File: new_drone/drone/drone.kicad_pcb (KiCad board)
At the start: 2 copper layers, 28 parts, among them J1 Conn_01x06, SW1 SW_Push_Open, SW2 SW_Push_Open, U1 MPU-6050, U2 ESP32-WROOM-32, U3 TPS63001, U4 BMP280, U5 MCP8063, U6 MCP8063, U7 MCP8063, U8 MCP8063

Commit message: add pcb cut
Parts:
- moved J1 15.4 mm to (161.3, 85.2), turned to 180 degrees
- moved U2 15.2 mm to (149.2, 79.4)
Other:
- board outline added: 100 x 100 mm
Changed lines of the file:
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@@
   )
   (footprint "RF_Module:ESP32-WROOM-32" (layer "F.Cu")
-    (at 134.431 75.699)
+    (at 149.155 79.385)
     (descr "Single 2.4 GHz Wi-Fi and Bluetooth combo chip https://www.espressif.com/sites/default/files/documentation/esp32-wroom-32_datasheet_en.pdf")
     (tags "Single 2.4 GHz Wi-Fi and Bluetooth combo  chip")
@@
       (polygon
         (pts
-          (xy 110.431 65.899)
-          (xy 158.431 65.899)
-          (xy 158.431 44.959)
-          (xy 110.431 44.959)
+          (xy 125.155 69.585)
+          (xy 173.155 69.585)
+          (xy 173.155 48.645)
+          (xy 125.155 48.645)
         )
       )
@@
   )
   (footprint "Connector_PinHeader_2.54mm:PinHeader_1x06_P2.54mm_Vertical" (layer "F.Cu")
-    (at 161.281 69.759)
+    (at 161.281 85.16 180)
     (descr "Through hole straight pin header, 1x06, 2.54mm pitch, single row")
     (tags "Through hole pin header THT 1x06 2.54mm single row")
@@
     (fp_line (start 1.27 13.97) (end -1.27 13.97)
       (stroke (width 0.1) (type solid)) (layer "F.Fab"))
-    (pad "1" thru_hole rect (at 0 0) (size 1.7 1.7) (drill 1) (layers "*.Cu" "*.Mask")
+    (pad "1" thru_hole rect (at 0 0 180) (size 1.7 1.7) (drill 1) (layers "*.Cu" "*.Mask")
       (net 1 "GND") (pinfunction "Pin_1") (pintype "passive"))
-    (pad "2" thru_hole oval (at 0 2.54) (size 1.7 1.7) (drill 1) (layers "*.Cu" "*.Mask")
+    (pad "2" thru_hole oval (at 0 2.54 180) (size 1.7 1.7) (drill 1) (layers "*.Cu" "*.Mask")
       (net 8 "unconnected-(J1-Pin_2-Pad2)") (pinfunction "Pin_2") (pintype "passive"))
-    (pad "3" thru_hole oval (at 0 5.08) (size 1.7 1.7) (drill 1) (layers "*.Cu" "*.Mask")
+    (pad "3" thru_hole oval (at 0 5.08 180) (size 1.7 1.7) (drill 1) (layers "*.Cu" "*.Mask")
       (net 2 "VCC") (pinfunction "Pin_3") (pintype "passive"))
-    (pad "4" thru_hole oval (at 0 7.62) (size 1.7 1.7) (drill 1) (layers "*.Cu" "*.Mask")
+    (pad "4" thru_hole oval (at 0 7.62 180) (size 1.7 1.7) (drill 1) (layers "*.Cu" "*.Mask")
       (net 9 "ESP_RX") (pinfunction "Pin_4") (pintype "passive"))
-    (pad "5" thru_hole oval (at 0 10.16) (size 1.7 1.7) (drill 1) (layers "*.Cu" "*.Mask")
+    (pad "5" thru_hole oval (at 0 10.16 180) (size 1.7 1.7) (drill 1) (layers "*.Cu" "*.Mask")
       (net 10 "ESP_TX") (pinfunction "Pin_5") (pintype "passive"))
-    (pad "6" thru_hole oval (at 0 12.7) (size 1.7 1.7) (drill 1) (layers "*.Cu" "*.Mask")
+    (pad "6" thru_hole oval (at 0 12.7 180) (size 1.7 1.7) (drill 1) (layers "*.Cu" "*.Mask")
       (net 11 "unconnected-(J1-Pin_6-Pad6)") (pinfunction "Pin_6") (pintype "passive"))
     (model "${KICAD6_3DMODEL_DIR}/Connector_PinHeader_2.54mm.3dshapes/PinHeader_1x06_P2.54mm_Vertical.wrl"
@@
     )
   )
+  (gr_line (start 100 145) (end 100 135)
+    (stroke (width 0.1) (type default)) (layer "Edge.Cuts"))
+  (gr_line (start 100 135) (end 120 115)
+    (stroke (width 0.1) (type default)) (layer "Edge.Cuts"))
+  (gr_line (start 200 65) (end 200 55)
+    (stroke (width 0.1) (type default)) (layer "Edge.Cuts"))
+  (gr_line (start 185 50) (end 165 70)
+    (stroke (width 0.1) (type default)) (layer "Edge.Cuts"))
+  (gr_line (start 200 55) (end 195 50)
+    (stroke (width 0.1) (type default)) (layer "Edge.Cuts"))
+  (gr_line (start 100 65) (end 100 55)
+    (stroke (width 0.1) (type default)) (layer "Edge.Cuts"))
+  (gr_line (start 200 145) (end 195 150)
+    (stroke (width 0.1) (type default)) (layer "Edge.Cuts"))
+  (gr_line (start 120 115) (end 120 85)
+    (stroke (width 0.1) (type default)) (layer "Edge.Cuts"))
+  (gr_line (start 135 70) (end 165 70)
+    (stroke (width 0.1) (type default)) (layer "Edge.Cuts"))
+  (gr_line (start 200 135) (end 200 145)
+    (stroke (width 0.1) (type default)) (layer "Edge.Cuts"))
+  (gr_line (start 180 85) (end 200 65)
+    (stroke (width 0.1) (type default)) (layer "Edge.Cuts"))
+  (gr_line (start 120 85) (end 100 65)
+    (stroke (width 0.1) (type default)) (layer "Edge.Cuts"))
+  (gr_line (start 105 50) (end 115 50)
+    (stroke (width 0.1) (type default)) (layer "Edge.Cuts"))
+  (gr_line (start 115 150) (end 105 150)
+    (stroke (width 0.1) (type default)) (layer "Edge.Cuts"))
+  (gr_line (start 105 150) (end 100 145)
+    (stroke (width 0.1) (type default)) (layer "Edge.Cuts"))
+  (gr_line (start 135 130) (end 115 150)
+    (stroke (width 0.1) (type default)) (layer "Edge.Cuts"))
+  (gr_line (start 180 115) (end 200 135)
+    (stroke (width 0.1) (type default)) (layer "Edge.Cuts"))
+  (gr_line (start 195 150) (end 185 150)
+    (stroke (width 0.1) (type default)) (layer "Edge.Cuts"))
+  (gr_line (start 100 55) (end 105 50)
+    (stroke (width 0.1) (type default)) (layer "Edge.Cuts"))
+  (gr_line (start 165 130) (end 135 130)
+    (stroke (width 0.1) (type default)) (layer "Edge.Cuts"))
+  (gr_line (start 195 50) (end 185 50)
+    (stroke (width 0.1) (type default)) (layer "Edge.Cuts"))
+  (gr_line (start 115 50) (end 135 70)
+    (stroke (width 0.1) (type default)) (layer "Edge.Cuts"))
+  (gr_line (start 185 150) (end 165 130)
+    (stroke (width 0.1) (type default)) (layer "Edge.Cuts"))
+  (gr_line (start 180 85) (end 180 115)
+    (stroke (width 0.1) (type default)) (layer "Edge.Cuts"))
   (gr_line (start 150 75) (end 175 50)
     (stroke (width 0.15) (type default)) (layer "User.1"))

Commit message: first wiring
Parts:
- removed R5: 100, Resistor_SMD:R_0603_1608Metric
- removed U3: TPS63001, Package_SON:Texas_DRC0010J_ThermalVias
- removed U6, U7, U8: MCP8063, Package_DFN_QFN:DFN-8-1EP_4x4mm_P0.8mm_EP2.5x3.6mm
- added TP1: TestPoint, TestPoint:TestPoint_Pad_3.0x3.0mm, F.Cu at (176.8, 73.3)
- added TP2: TestPoint, TestPoint:TestPoint_Pad_3.0x3.0mm, F.Cu at (180.3, 76.8)
- added TP3: TestPoint, TestPoint:TestPoint_Pad_3.0x3.0mm, F.Cu at (173.2, 69.7)
- C4, C5, C6: value 0.1uF -> C
- D1: moved to B.Cu
- moved C1 45.7 mm to (155.5, 101.8), turned to 180 degrees
- moved C2 44.6 mm to (155.5, 100.0)
- moved C3 43.9 mm to (155.5, 98.2)
- moved R7 35.0 mm to (154.8, 94.1), turned to -90 degrees
- moved R6 33.6 mm to (153.0, 94.1), turned to -90 degrees
- moved U5 32.4 mm to (171.3, 78.4), turned to -135 degrees
- moved C5 31.6 mm to (136.8, 117.5)
- moved C4 31.6 mm to (136.8, 115.0)
- moved C6 31.6 mm to (136.8, 120.0)
- moved R1 31.6 mm to (140.8, 110.0)
- moved R4 31.6 mm to (140.8, 117.5)
- moved C7 31.6 mm to (140.8, 107.5)
- moved R2 31.6 mm to (140.8, 112.5)
- moved R3 31.6 mm to (140.8, 115.0)
- moved D1 21.5 mm to (150.0, 72.9), turned to 180 degrees
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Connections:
- C4 pad 1: Net-(U3-EN) -> +BATT
- C5 pad 1: VCC -> +BATT
- C6 pad 1: VCC -> Net-(U5-Vbias)
- U5 pad 2: unconnected-(U5-Vbias-Pad2) -> Net-(U5-Vbias)
- U5 pad 3: unconnected-(U5-OUT1-Pad3) -> Net-(U5-OUT1)
- U5 pad 4: unconnected-(U5-OUT2-Pad4) -> Net-(U5-OUT2)
- U5 pad 5: unconnected-(U5-GND-Pad5) -> GND
- U5 pad 6: unconnected-(U5-OUT3-Pad6) -> Net-(U5-OUT3)
- U5 pad 7: unconnected-(U5-VDD-Pad7) -> +BATT
- U5 pad 8: unconnected-(U5-PWM-Pad8) -> MOTOR_1
- U5 pad 9: unconnected-(U5-GND-Pad9) -> GND
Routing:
- net VCC: track 0.00 -> 14.2 mm, vias 0 -> 2
- net Net-(U5-OUT3): track 0.00 -> 14.0 mm, vias 0 -> 2
- net Net-(U5-OUT1): track 0.00 -> 9.38 mm
- net Net-(U1-REGOUT): track 0.00 -> 9.14 mm
- net Net-(U5-OUT2): track 0.00 -> 6.93 mm
- net Net-(U4-SDO): track 0.00 -> 6.66 mm
- net SDA: track 0.00 -> 5.54 mm
- net Net-(U1-CPOUT): track 0.00 -> 4.77 mm
- net ESP_RX: track 0.00 -> 3.68 mm
- net ESP_TX: track 0.00 -> 3.41 mm
- net SCL: track 0.00 -> 3.35 mm
- net Net-(U4-CSB): track 0.00 -> 3.10 mm
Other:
- outline, holes or cut-outs redrawn

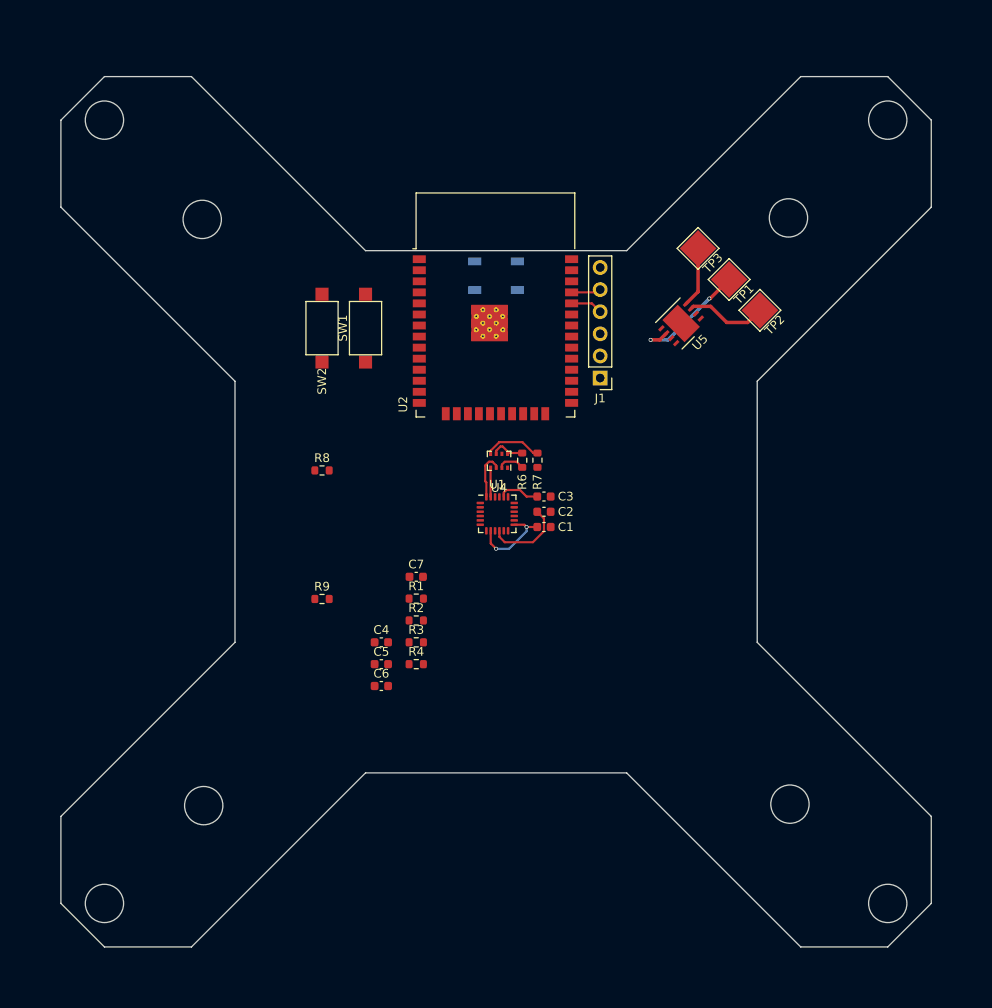
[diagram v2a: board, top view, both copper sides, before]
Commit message: add regulator
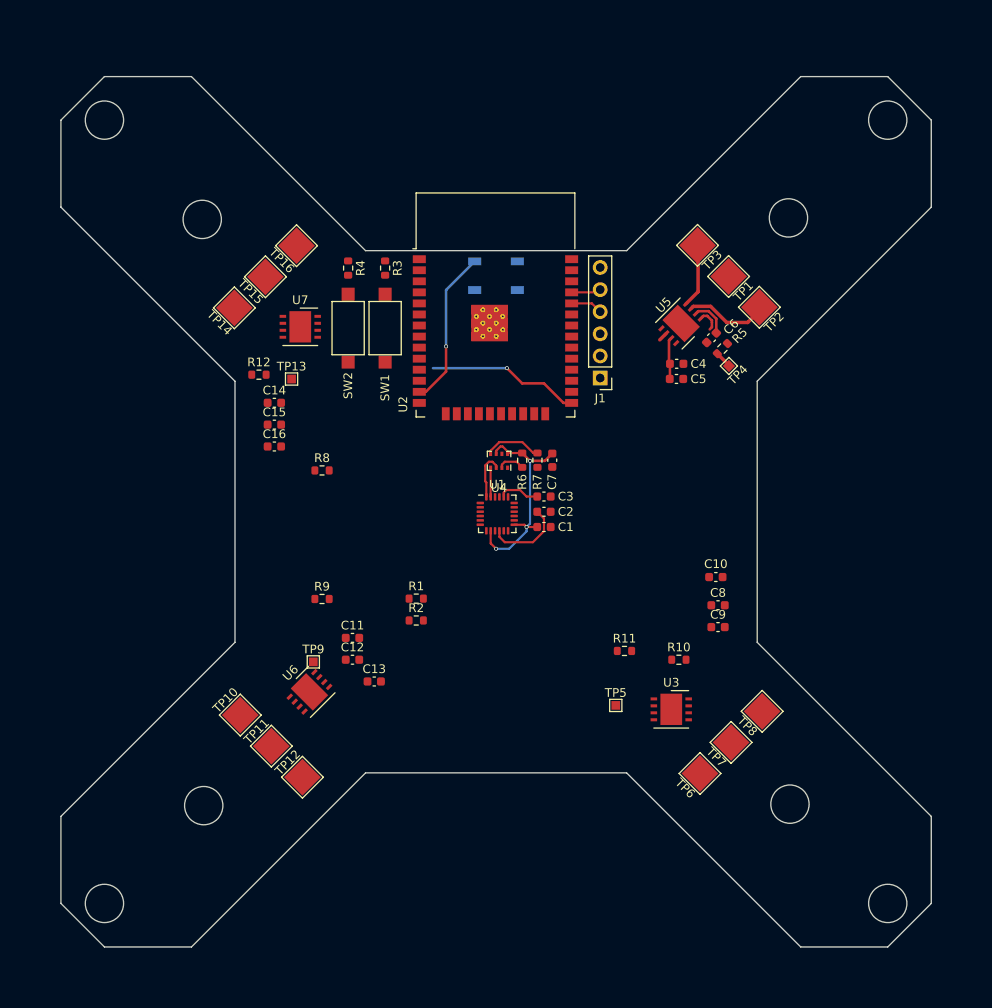
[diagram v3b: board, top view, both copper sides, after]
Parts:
- added C10: C, Capacitor_SMD:C_0603_1608Metric, F.Cu at (175.2, 107.5)
- added C11: C, Capacitor_SMD:C_0603_1608Metric, F.Cu at (133.5, 114.5)
- added C12: C, Capacitor_SMD:C_0603_1608Metric, F.Cu at (133.5, 117.0)
- added C13: C, Capacitor_SMD:C_0603_1608Metric, F.Cu at (136.0, 119.5)
- added C14: C, Capacitor_SMD:C_0603_1608Metric, F.Cu at (124.5, 87.5)
- added C15: C, Capacitor_SMD:C_0603_1608Metric, F.Cu at (124.5, 90.0)
- added C16: C, Capacitor_SMD:C_0603_1608Metric, F.Cu at (124.5, 92.5)
- added C8: C, Capacitor_SMD:C_0603_1608Metric, F.Cu at (175.5, 110.7)
- added C9: C, Capacitor_SMD:C_0603_1608Metric, F.Cu at (175.5, 113.2)
- added R10: 10K, Resistor_SMD:R_0603_1608Metric, F.Cu at (171.0, 117.0)
- added R11: 10K, Resistor_SMD:R_0603_1608Metric, F.Cu at (164.8, 116.0)
- added R12: 10K, Resistor_SMD:R_0603_1608Metric, F.Cu at (122.8, 84.2)
- added R5: 10K, Resistor_SMD:R_0603_1608Metric, F.Cu at (176.0, 81.2)
- added TP10: TestPoint, TestPoint:TestPoint_Pad_3.0x3.0mm, F.Cu at (120.6, 123.4)
- added TP11: TestPoint, TestPoint:TestPoint_Pad_3.0x3.0mm, F.Cu at (124.2, 126.9)
- added TP12: TestPoint, TestPoint:TestPoint_Pad_3.0x3.0mm, F.Cu at (127.8, 130.5)
- added TP13: TestPoint, TestPoint:TestPoint_Pad_1.0x1.0mm, F.Cu at (126.5, 84.8)
- added TP14: TestPoint, TestPoint:TestPoint_Pad_3.0x3.0mm, F.Cu at (119.9, 76.6)
- added TP15: TestPoint, TestPoint:TestPoint_Pad_3.0x3.0mm, F.Cu at (123.5, 73.0)
- added TP16: TestPoint, TestPoint:TestPoint_Pad_3.0x3.0mm, F.Cu at (127.1, 69.4)
- added TP4: TestPoint, TestPoint:TestPoint_Pad_1.0x1.0mm, F.Cu at (176.8, 83.2)
- added TP5: TestPoint, TestPoint:TestPoint_Pad_1.0x1.0mm, F.Cu at (163.8, 122.2)
- added TP6: TestPoint, TestPoint:TestPoint_Pad_3.0x3.0mm, F.Cu at (173.4, 130.1)
- added TP7: TestPoint, TestPoint:TestPoint_Pad_3.0x3.0mm, F.Cu at (177.0, 126.5)
- added TP8: TestPoint, TestPoint:TestPoint_Pad_3.0x3.0mm, F.Cu at (180.6, 122.9)
- added TP9: TestPoint, TestPoint:TestPoint_Pad_1.0x1.0mm, F.Cu at (129.0, 117.2)
- added U3: MCP8063, Package_DFN_QFN:DFN-8-1EP_4x4mm_P0.8mm_EP2.5x3.6mm, F.Cu at (170.1, 122.7)
- added U6: MCP8063, Package_DFN_QFN:DFN-8-1EP_4x4mm_P0.8mm_EP2.5x3.6mm, F.Cu at (128.6, 120.7)
- added U7: MCP8063, Package_DFN_QFN:DFN-8-1EP_4x4mm_P0.8mm_EP2.5x3.6mm, F.Cu at (127.5, 78.8)
- moved C6 55.1 mm to (174.8, 80.0), turned to -135 degrees
- moved C5 47.2 mm to (170.7, 84.7)
- moved C4 46.6 mm to (170.8, 83.0)
- moved R4 46.2 mm to (133.0, 72.0), turned to -90 degrees
- moved R3 43.1 mm to (137.2, 72.0), turned to -90 degrees
- moved C7 20.6 mm to (156.5, 94.1), turned to -90 degrees
- moved SW2 3.00 mm to (133.0, 78.9)
- moved SW1 2.25 mm to (137.2, 78.9)
- moved TP1 0.35 mm to (176.7, 73.0)
- moved TP2 0.35 mm to (180.2, 76.5)
- moved TP3 0.35 mm to (173.1, 69.4)
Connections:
- R8 pad 1: BAT+ -> +BATT
- U5 pad 1: unconnected-(U5-FG-Pad1) -> Net-(U5-FG)
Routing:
- net Net-(D1-DIN): track 0.00 -> 18.1 mm, vias 0 -> 1
- net Net-(SW2-A): track 0.00 -> 17.6 mm, vias 0 -> 1
- net Net-(U5-OUT3): track 14.0 -> 1.07 mm, vias 2 -> 0
- net VCC: track 14.2 -> 26.2 mm, vias 2 -> 3
- net +BATT: track 0.00 -> 4.85 mm
- net Net-(U5-FG): track 0.00 -> 4.71 mm
- net Net-(U5-Vbias): track 0.00 -> 4.45 mm

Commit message: add regulator + xt60 connector
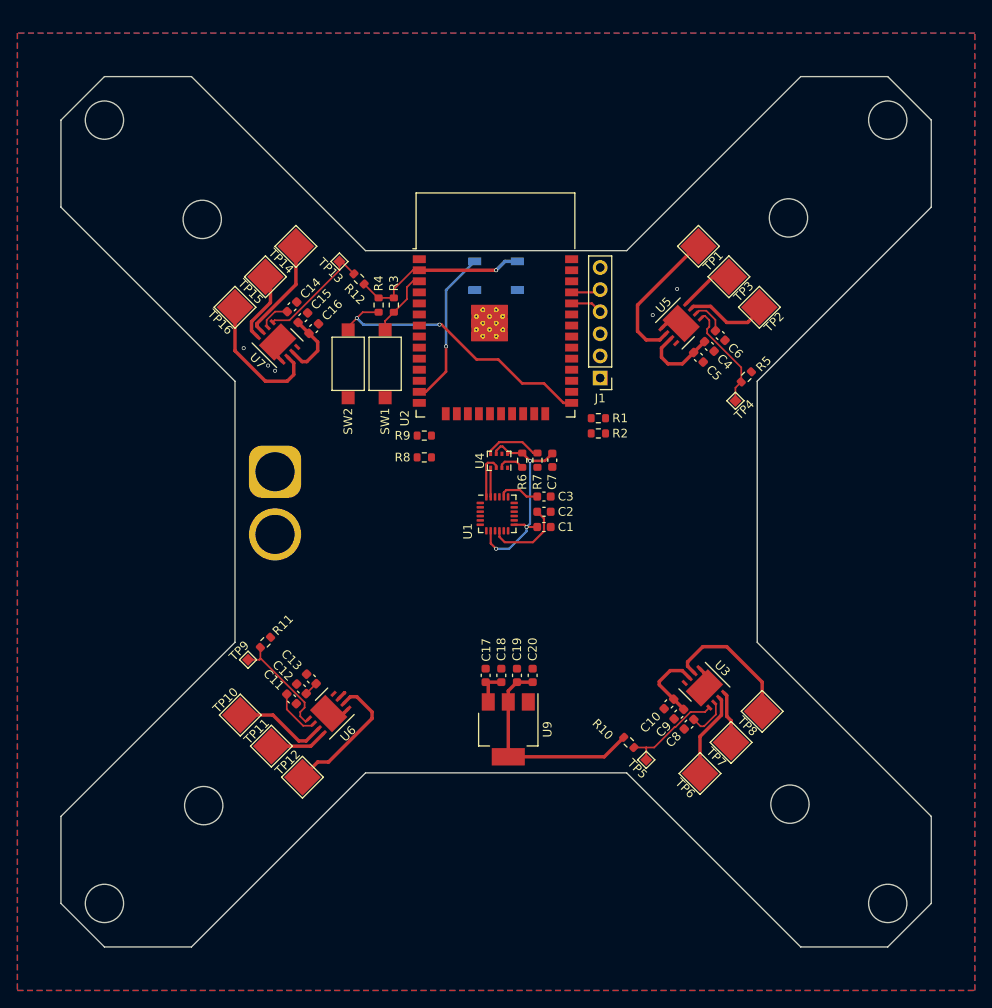
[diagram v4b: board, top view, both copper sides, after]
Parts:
- added C17: C, Capacitor_SMD:C_0603_1608Metric, F.Cu at (148.8, 118.8)
- added C18: C, Capacitor_SMD:C_0603_1608Metric, F.Cu at (150.6, 118.8)
- added C19: C, Capacitor_SMD:C_0603_1608Metric, F.Cu at (152.4, 118.8)
- added C20: C, Capacitor_SMD:C_0603_1608Metric, F.Cu at (154.2, 118.8)
- added J2: XT60-M, Connector_AMASS:AMASS_XT60-M_1x02_P7.20mm_Vertical, B.Cu at (124.6, 95.4)
- added U9: LM1117MP-3.3, Package_TO_SOT_SMD:SOT-223-3_TabPin2, F.Cu at (151.4, 125.0)
- moved R11 41.3 mm to (123.5, 115.0), turned to -135 degrees
- moved R2 30.0 mm to (161.8, 91.0), turned to 180 degrees
- moved R1 29.5 mm to (161.8, 89.2)
- moved R9 22.1 mm to (141.8, 91.2)
- moved R12 15.9 mm to (134.2, 73.2), turned to 135 degrees
- moved C10 15.5 mm to (169.9, 122.1), turned to -135 degrees
- moved TP13 14.6 mm to (132.0, 71.2), turned to 135 degrees
- moved C16 14.3 mm to (129.0, 79.0), turned to 45 degrees
- moved C8 14.1 mm to (172.2, 124.4), turned to -135 degrees
- moved C15 12.7 mm to (127.8, 77.7), turned to 45 degrees
- moved R8 11.8 mm to (141.8, 93.8)
- moved C14 11.2 mm to (126.5, 76.5), turned to 45 degrees
- moved R10 11.1 mm to (165.2, 126.5), turned to -45 degrees
- moved C9 11.0 mm to (171.0, 123.2), turned to -135 degrees
- moved TP14 10.00 mm to (127.0, 69.5)
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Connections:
- C1 pad 2: VCC -> +3.3V
- C7 pad 1: VCC -> +3.3V
- D1 pad 1: VCC -> +3.3V
- R1 pad 1: VCC -> +3.3V
- R2 pad 1: VCC -> +3.3V
- R3 pad 1: VCC -> +3.3V
- R4 pad 1: VCC -> +3.3V
- R6 pad 1: VCC -> +3.3V
- U1 pad 13: VCC -> +3.3V
- U1 pad 8: VCC -> +3.3V
- U2 pad 2: VCC -> +3.3V
- U4 pad 6: VCC -> +3.3V
- U4 pad 8: VCC -> +3.3V
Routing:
- net +3.3V: track 0.00 -> 71.8 mm, vias 0 -> 4
- net +BATT: track 4.85 -> 32.6 mm
- net VCC: track 26.2 -> 0.00 mm, vias 3 -> 0
- net Net-(U3-OUT3): track 0.00 -> 16.0 mm
- net Net-(U6-OUT3): track 0.00 -> 15.9 mm
- net Net-(U7-OUT3): track 0.00 -> 15.9 mm
- net Net-(U5-OUT3): track 1.07 -> 16.8 mm
- net Net-(SW2-A): track 17.6 -> 33.3 mm, vias 1 -> 2
- net Net-(U7-FG): track 0.00 -> 13.4 mm
- net Net-(U6-FG): track 0.00 -> 13.2 mm
- net Net-(U3-FG): track 0.00 -> 12.0 mm
- net Net-(U7-OUT1): track 0.00 -> 11.9 mm
- net Net-(U6-OUT1): track 0.00 -> 10.9 mm
- net GND: track 0.00 -> 9.99 mm, vias 0 -> 5
- net Net-(U3-OUT1): track 0.00 -> 9.83 mm
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- added copper zone on B.Cu, net GND
- added copper zone on F.Cu, net GND
